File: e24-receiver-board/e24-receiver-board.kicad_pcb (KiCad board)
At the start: 2 copper layers, 24 x 8.6 mm, 21 parts, among them J1 505070-2422, J10 SPEAKER-, J11 GND1, J12 TRACK_RIGHT, J13 MOTOR+, J14 U+, J15 VCC, J16 LAMP_REAR, J17 AUX2, J18 AUX4, J19 AUX11, J2 TRACK_LEFT, J20 SPEAKER+, J21 GND2, J3 MOTOR-, J4 LAMP_FRONT, J5 CAP+, J6 AUX1, J7 AUX3, J8 AUX10, J9 AUX12

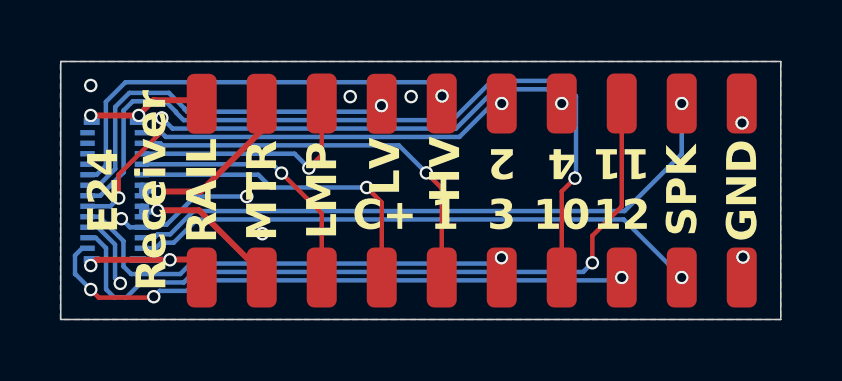
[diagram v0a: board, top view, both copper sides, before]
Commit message: fix: space out higher power terminals
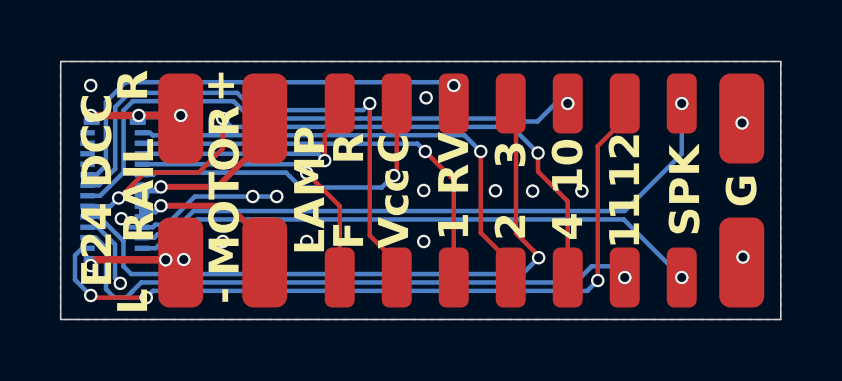
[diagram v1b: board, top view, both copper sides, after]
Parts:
- J11, J12, J13, J2, J21, J3: footprint Connector_Wire:SolderWirePad_1x01_SMD_1x2mm -> Local Library:SolderWirePad_1x01_SMD_1.5x3mm
- moved J15 5.82 mm to (141.2, 66.8)
- moved J5 5.81 mm to (141.2, 72.5)
- moved J17 5.81 mm to (145.1, 66.8)
- moved J7 5.81 mm to (145.1, 72.5)
- moved J18 5.80 mm to (146.9, 66.8)
- moved J8 5.80 mm to (146.9, 72.5)
- moved J19 5.80 mm to (148.8, 66.8)
- moved J9 5.80 mm to (148.8, 72.5)
- moved J2 0.86 mm to (134.1, 72.0)
- moved J12 0.85 mm to (134.1, 67.2)
- moved J14 0.60 mm to (139.3, 66.8)
- moved J4 0.60 mm to (139.3, 72.5)
- moved J3 0.51 mm to (136.8, 72.0)
- moved J13 0.50 mm to (136.8, 67.2)
- moved J11 0.50 mm to (152.8, 72.0)
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- renumbered J16 to J14, J5 to J15, J14 to J16, J7 to J17, J8 to J18, J9 to J19, J15 to J5, J17 to J7, J18 to J8, J19 to J9
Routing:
- net /AUX10: track 26.1 -> 19.2 mm
- net /AUX3: track 15.3 -> 21.8 mm
- net VCC: track 12.6 -> 18.4 mm
- net /AUX12: track 20.0 -> 25.5 mm
- net /AUX11: track 24.7 -> 20.1 mm
- net /AUX2 (VDC): track 12.5 -> 16.2 mm
- net /AUX4: track 18.6 -> 21.9 mm
- net GND: track 7.25 -> 8.25 mm, vias 9 -> 15
- net /LAMP_FRONT: track 8.81 -> 9.55 mm
- net /TRACK_LEFT: track 5.44 -> 4.83 mm, vias 2 -> 3
- net /AUX1 (VDC): track 13.6 -> 14.2 mm
- net /TRACK_RIGHT: track 4.40 -> 4.94 mm, vias 2 -> 3
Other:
- board text added: "+"
- board text added: "-"
- board text added: "C"
- board text added: "E24 Adapter"
- board text added: "E24 DCC"
- board text added: "F"
- board text added: "G"
- board text added: "L"
- board text added: "LAMP"
- board text added: "MOTOR"
- board text added: "R"
- board text added: "RV"
- board text added: "Vcc"
- board text removed: "C+"
- board text removed: "E24 Receiver"
- board text removed: "GND"
- board text removed: "HV"
- board text removed: "LMP"
- board text removed: "LV"
- board text removed: "MTR"
